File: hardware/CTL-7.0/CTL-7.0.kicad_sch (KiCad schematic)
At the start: 18 parts, among them J2 Left, J3 Right, U1 STM32H750VBTx, U2 AMS1117-3.3, Y1 32.768K, Y2 25MHz

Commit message: modified:   Ferrite Transformer Calculation.xlsx 	modified:   archive/Peripheral Migration ESP32S3-STM32H7.md 	renamed:    archive/PR_ 0201_2026.docx -> archive/Purchase 20260201.docx 	new file:   archive/Purchase 20260720.docx 	new file:   archive/Purchase Plan/bom.csv 	new file:   archive/Purchase Plan/bom.xlsx 	new file:   archive/Purchase Recaps.xlsx 	modified:   archive/REM - Vsense.xlsx 	new file:   archive/datasheets/SPC7040.PDF 	new file:   archive/datasheets/rm0433-stm32h742-stm32h743-753-and-stm32h750-value-line-advanced-armbased-32bit-mcus-stmicroelectronics.pdf 	new file:   archive/refferences/MiniSTM32H7xx-master/.gitattributes 	new file:   archive/refferences/MiniSTM32H7xx-master/.gitignore 	new file:   archive/refferences/MiniSTM32H7xx-master/Datasheet/MCU/DM00287603_ZHV2.pdf 	new file:   "archive/refferences/MiniSTM32H7xx-master/Datasheet/MCU/ES0396_STM32H750xB\345\222\214STM32H753xI\345\215\225\347\211\207\346\234\272\347\232\204\345\261\200\351\231\220\346\200\247.pdf" 	new file:   "archive/refferences/MiniSTM32H7xx-master/Datasheet/MCU/PM0253_STM32F7\345\222\214 STM32H7\345\215\225\347\211\207\346\234\272\347\274\226\347\250\213\346\211\213\345\206\214.pdf" 	new file:   "archive/refferences/MiniSTM32H7xx-master/Datasheet/MCU/RM0433_STM32H7x3\345\222\214STM32H750\345\215\225\347\211\207\346\234\272\345\217\202\350\200\203\346\211\213\345\206\214.pdf" 	new file:   archive/refferences/MiniSTM32H7xx-master/Datasheet/MCU/STM32H743VI_Datasheet.pdf 	new file:   archive/refferences/MiniSTM32H7xx-master/Datasheet/MCU/STM32H750VB_Datasheet.pdf 	new file:   archive/refferences/MiniSTM32H7xx-master/Datasheet/MKESD0402MS05.PDF 	new file:   archive/refferences/MiniSTM32H7xx-master/Datasheet/ST7735S_V1.5_20150303.pdf 	new file:   archive/refferences/MiniSTM32H7xx-master/Datasheet/SY8088AAC.PDF 	new file:   archive/refferences/MiniSTM32H7xx-master/Datasheet/Sensor/OV2640-camera module.pdf 	new file:   archive/refferences/MiniSTM32H7xx-master/Datasheet/Sensor/OV26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
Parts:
- removed C1, C3: 10u, Capacitor_Tantalum_SMD:CP_EIA-3528-12_Kemet-T, symbol Device:C_Polarized
- removed C2, C4: 100n, Capacitor_SMD:C_0805_2012Metric, symbol Device:C
- removed C5, C6: 10p, Capacitor_SMD:C_0805_2012Metric, symbol Device:C
- removed C7, C8: 20p, Capacitor_SMD:C_0805_2012Metric, symbol Device:C
- removed H1, H2, H3, H4: MountingHole_Pad, MountingHole:MountingHole_3mm_Pad, symbol Mechanical:MountingHole_Pad
- removed J2: Left, Connector_PinHeader_2.54mm:PinHeader_2x22_P2.54mm_Vertical, symbol Connector_Generic:Conn_02x22_Odd_Even
- removed J3: Right, Connector_PinHeader_2.54mm:PinHeader_2x22_P2.54mm_Vertical, symbol Connector_Generic:Conn_02x22_Odd_Even
- removed U1: STM32H750VBTx, Package_QFP:LQFP-100_14x14mm_P0.5mm, symbol MCU_ST_STM32H7:STM32H750VBTx
- removed U2: AMS1117-3.3, Package_TO_SOT_SMD:SOT-223-3_TabPin2, symbol Regulator_Linear:AMS1117-3.3
- removed Y1: 32.768K, Crystal:Crystal_SMD_3215-2Pin_3.2x1.5mm, symbol Device:Crystal
- removed Y2: 25MHz, Crystal:Crystal_SMD_5032-2Pin_5.0x3.2mm, symbol Device:Crystal
- added U1: H750, Core:STM32H750_v1, symbol core:STM32H750VBTx
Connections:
- net GND: now also U1.10 (GND), U1.19 (GND), U1.26 (GND), U1.49 (GND), U1.74 (GND), U1.99 (GND)
- new net: U1.100 (+3.3V_OUT), U1.11 (+3.3V_OUT), U1.27 (+3.3V_OUT), U1.75 (+3.3V_OUT)
- new net CTL_RLY1: U1.29 (A.05)
- new net CTL_RLY2: U1.30 (A.06)
- new net MSD1: U1.24 (A.02)
- new net MSD2: U1.25 (A.03)
- new net OPTO: U1.28 (A.04)
- new net PWM_EN: U1.31 (A.07)
- new net SENS_COAG: U1.23 (A.01)
- new net SENS_CUT: U1.22 (A.00)

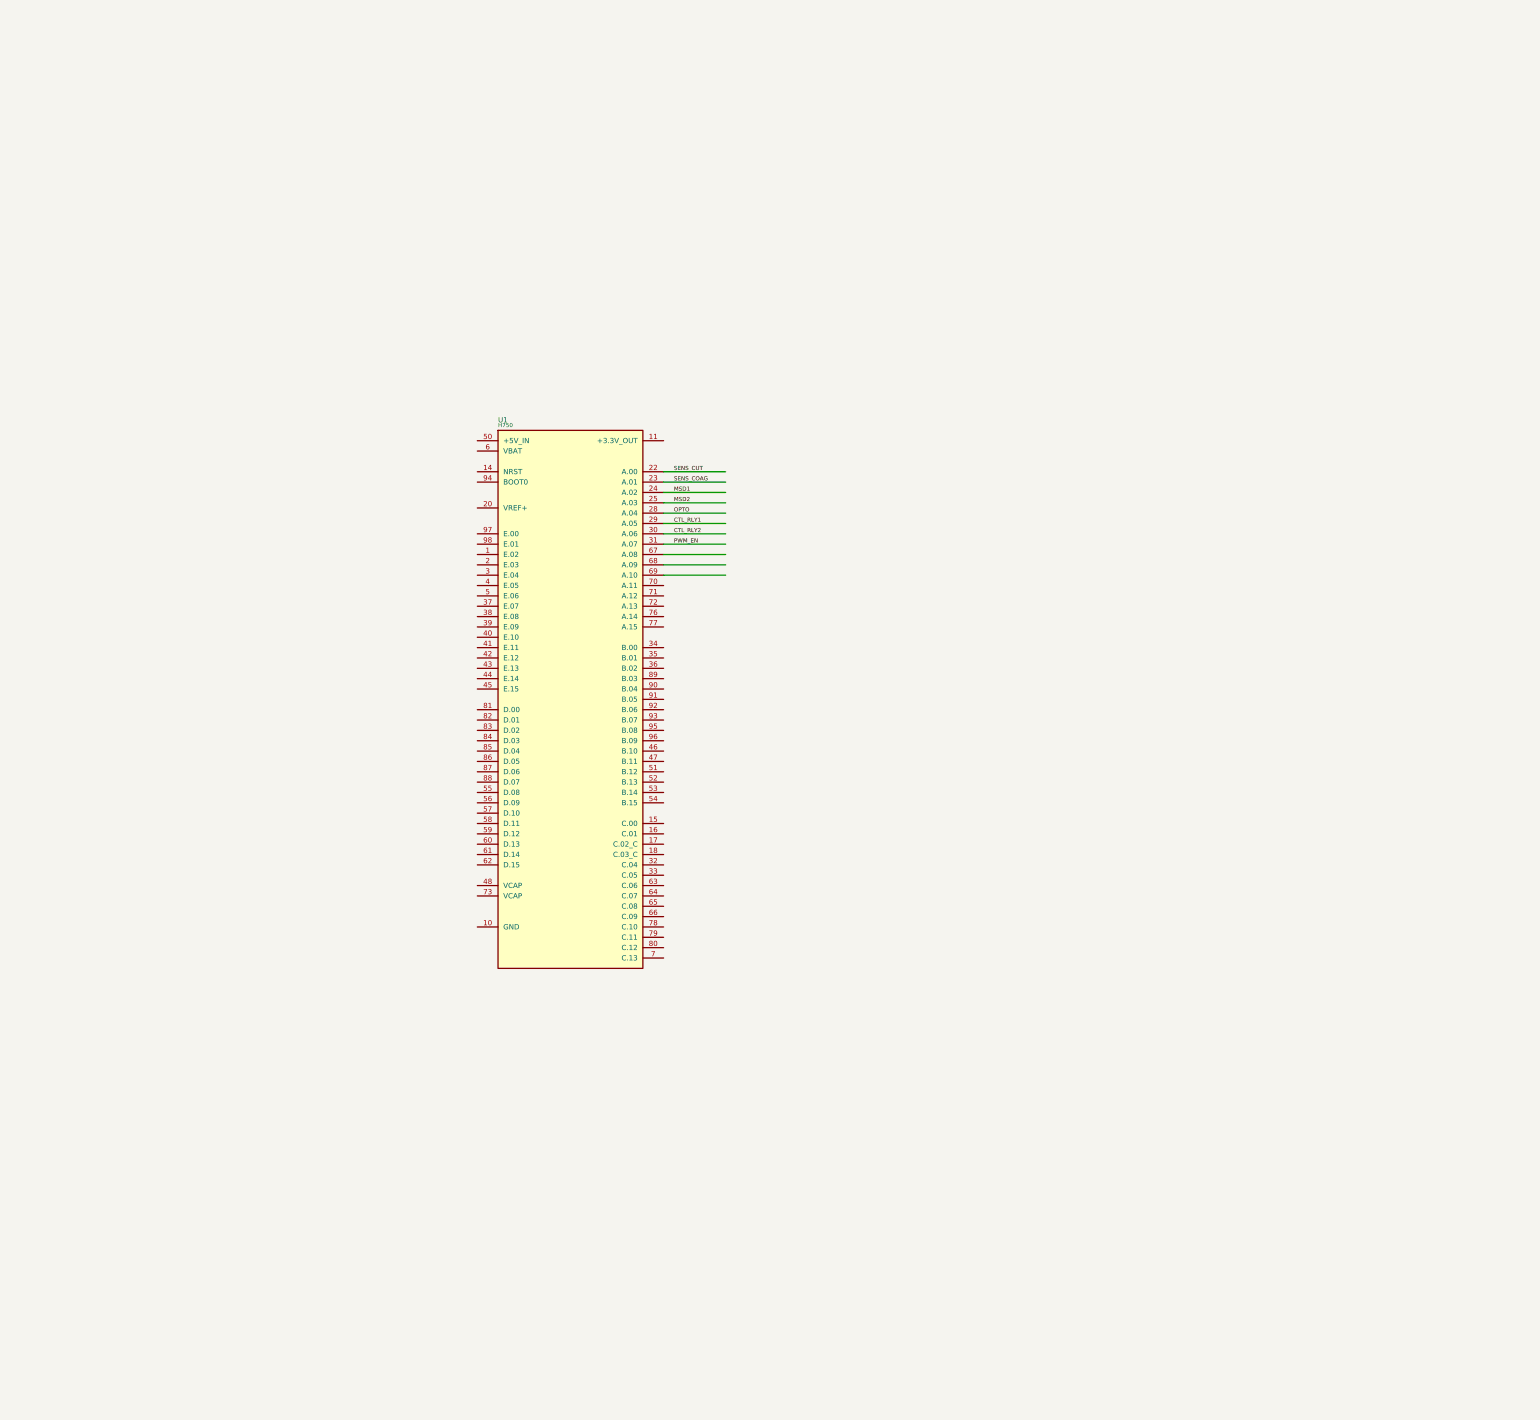
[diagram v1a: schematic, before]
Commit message: modified:   archive/Peripheral Migration ESP32S3-STM32H7.md 	new file:   archive/refferences/STM32H750xB pin definition.xlsx 	new file:   archive/refferences/STM32H750xB_pin_definition-TIM_LPTIM_HRTIM.xlsx 	new file:   archive/refferences/pin alternatives.xlsx 	new file:   firmware/core-h750/.cproject 	new file:   firmware/core-h750/.mxproject 	new file:   firmware/core-h750/.osx.project 	new file:   firmware/core-h750/.project 	new file:   firmware/core-h750/.settings/language.settings.xml 	new file:   firmware/core-h750/.settings/org.eclipse.core.resources.prefs 	new file:   firmware/core-h750/.settings/stm32cubeide.project.prefs 	new file:   firmware/core-h750/Debug/Drivers/STM32H7xx_HAL_Driver/Src/stm32h7xx_hal.cyclo 	new file:   firmware/core-h750/Debug/Drivers/STM32H7xx_HAL_Driver/Src/stm32h7xx_hal.su 	new file:   firmware/core-h750/Debug/Drivers/STM32H7xx_HAL_Driver/Src/stm32h7xx_hal_cortex.cyclo 	new file:   firmware/core-h750/Debug/Drivers/STM32H7xx_HAL_Driver/Src/stm32h7xx_hal_cortex.su 	new file:   firmware/core-h750/Debug/Drivers/STM32H7xx_HAL_Driver/Src/stm32h7xx_hal_dma.cyclo 	new file:   firmware/core-h750/Debug/Drivers/STM32H7xx_HAL_Driver/Src/stm32h7xx_hal_dma.su 	new file:   firmware/core-h750/Debug/Drivers/STM32H7xx_HAL_Driver/Src/stm32h7xx_hal_dma_ex.cyclo 	new file:   firmware/core-h750/Debug/Drivers/STM32H7xx_HAL_Driver/Src/stm32h7xx_hal_dma_ex.su 	new file:   firmware/core-h750/Debug/Drivers/STM32H7xx_HAL_Driver/Src/stm32h7xx_hal_exti.cyclo 	new file:   firmware/core-h750/Debug/Drivers/STM32H7xx_HAL_Driver/Src/stm32h7xx_hal_exti.su 	new file:   firmware/core-h750/Debug/Drivers/STM32H7xx_HAL_Driver/Src/stm32h7xx_hal_flash.cyclo 	new file:   firmware/core-h750/Debug/Drivers/STM32H7xx_HAL_Driver/Src/stm32h7xx_hal_flash.su 	new file:   firmware/core-h750/Debug/Drivers/STM32H7xx_HAL_Driver/Src/stm32h7xx_hal_flash_ex.cyclo 	new file:   firmware/core-h750/Debug/Drivers/STM32H7xx_HAL_Driver/Src/stm32h7xx_hal_flash_ex.su 	new file:   firmware/core-h750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
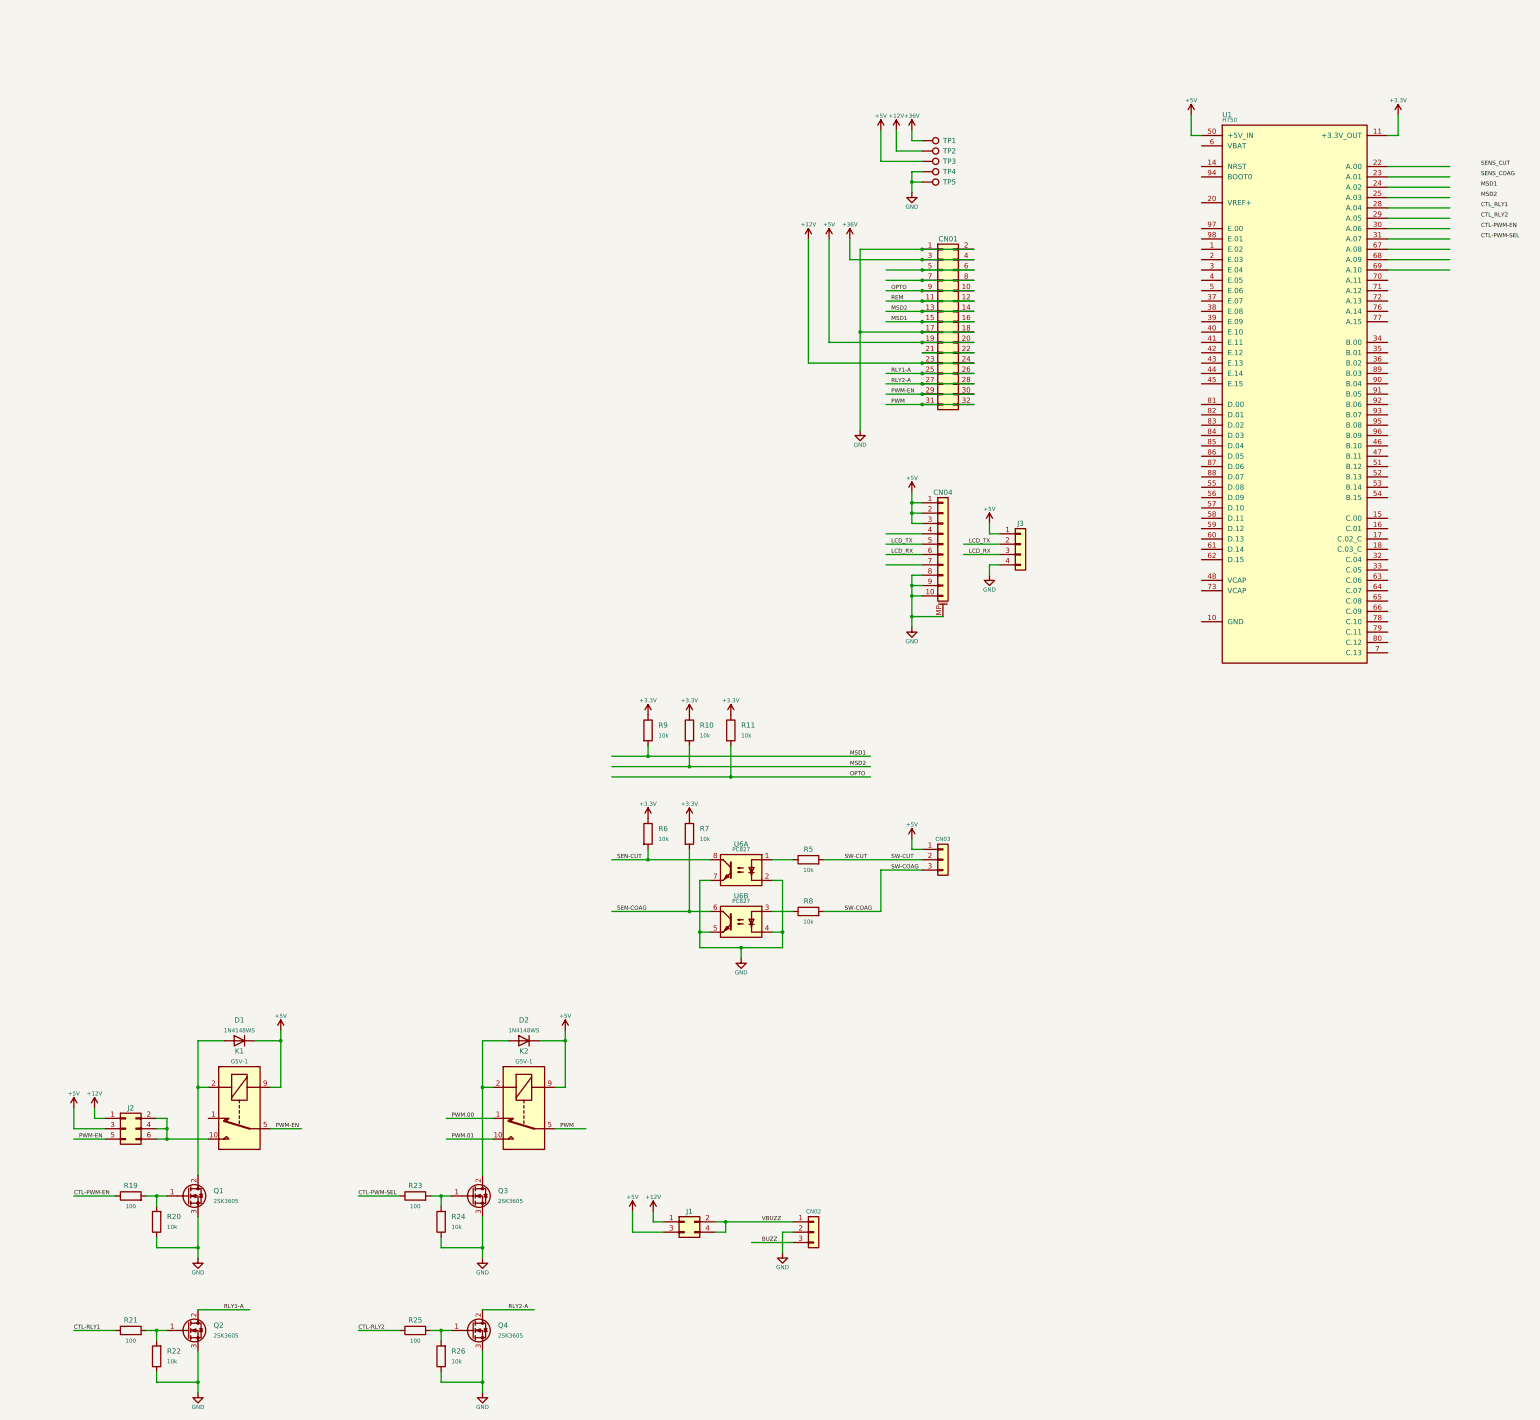
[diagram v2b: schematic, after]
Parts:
- added CN01: Conn_02x16_Odd_Even, Connector_PinHeader_2.54mm:PinHeader_2x16_P2.54mm_Vertical, symbol Connector_Generic:Conn_02x16_Odd_Even
- added CN02, CN03: Conn_01x03, Connector_JST:JST_XH_B3B-XH-A_1x03_P2.50mm_Vertical, symbol Connector_Generic:Conn_01x03
- added CN04: (no value), Connector_FFC-FPC:TE_1-84952-0_1x10-1MP_P1.0mm_Horizontal, symbol Connector_Generic_MountingPin:Conn_01x10_MountingPin
- added D1, D2: 1N4148WS, Diode_SMD:D_SOD-323, symbol Diode:1N4148WS
- added J1: Conn_02x02_Odd_Even, Connector_PinHeader_2.54mm:PinHeader_2x02_P2.54mm_Vertical_SMD, symbol Connector_Generic:Conn_02x02_Odd_Even
- added J2: Conn_02x03_Odd_Even, Connector_PinHeader_2.54mm:PinHeader_2x03_P2.54mm_Vertical_SMD, symbol Connector_Generic:Conn_02x03_Odd_Even
- added J3: Conn_01x04, Connector_PinHeader_2.54mm:PinHeader_1x04_P2.54mm_Vertical, symbol Connector_Generic:Conn_01x04
- added K1, K2: G5V-1, Relay_THT:Relay_SPDT_Omron_G5V-1, symbol Relay:G5V-1
- added Q1, Q2, Q3, Q4: 2SK3605, Package_TO_SOT_SMD:SOT-89-3, symbol Transistor_FET:2SK3065
- added R10, R11, R20, R22, R24, R26, R5, R6, R7, R8, R9: 10k, Resistor_SMD:R_0805_2012Metric, symbol Device:R
- added R19, R21, R23, R25: 100, Resistor_SMD:R_0805_2012Metric, symbol Device:R
- added TP1, TP2, TP3, TP4, TP5: TestPoint, TestPoint:TestPoint_THTPad_2.2225x2.2225mm_Drill1.5mm, symbol Connector:TestPoint
- added U6: PC827, Package_DIP:DIP-8_W7.62mm_Socket, symbol Isolator:PC827
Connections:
- net CTL_RLY1: no longer U1.29 (A.05)
- net CTL_RLY2: no longer U1.30 (A.06)
- net GND: now also CN01.1 (Pin_1), CN01.17 (Pin_17), CN01.18 (Pin_18), CN01.2 (Pin_2), CN02.2 (Pin_2), CN04.10 (Pin_10), CN04.8 (Pin_8), CN04.9 (Pin_9), CN04.MP (MountPin), J3.4 (Pin_4), Q1.3 (S), Q2.3 (S), Q3.3 (S), Q4.3 (S), R20.1, R22.1, R24.1, R26.1, TP4.1, TP5.1, U6.2, U6.4, U6.5, U6.7
- net MSD1: now also CN01.15 (Pin_15), CN01.16 (Pin_16), R9.2; no longer U1.24 (A.02)
- net MSD2: now also CN01.13 (Pin_13), CN01.14 (Pin_14), R10.2; no longer U1.25 (A.03)
- net OPTO: now also CN01.10 (Pin_10), CN01.9 (Pin_9), R11.2; no longer U1.28 (A.04)
- net SENS_COAG: no longer U1.23 (A.01)
- net SENS_CUT: no longer U1.22 (A.00)
- net +3.3V: now reaches U1.100 (+3.3V_OUT), U1.11 (+3.3V_OUT), U1.27 (+3.3V_OUT), U1.75 (+3.3V_OUT)
- net +3.3V: now also R10.1, R11.1, R6.1, R7.1, R9.1
- net +5V: now reaches U1.50 (+5V_IN)
- net +5V: now also CN01.19 (Pin_19), CN01.20 (Pin_20), CN03.1 (Pin_1), CN04.1 (Pin_1), CN04.2 (Pin_2), CN04.3 (Pin_3), D1.1 (K), D2.1 (K), J1.3 (Pin_3), J2.3 (Pin_3), J3.1 (Pin_1), K1.9, K2.9, TP3.1
- net PWM_EN: no longer names the net of U1.31 (A.07)
- new net: D2.2 (A), K2.2, Q3.2 (D)
- new net: CN01.21 (Pin_21), CN01.22 (Pin_22)
- new net: CN01.5 (Pin_5), CN01.6 (Pin_6)
- new net: CN01.7 (Pin_7), CN01.8 (Pin_8)
- new net: Q3.1 (G), R23.2, R24.2
- new net: Q4.1 (G), R25.2, R26.2
- new net: R8.1, U6.3
- new net: R5.1, U6.1
- new net: Q1.1 (G), R19.2, R20.2
- new net: Q2.1 (G), R21.2, R22.2
- new net: D1.2 (A), K1.2, Q1.2 (D)
- new net: J2.2 (Pin_2), J2.4 (Pin_4), J2.6 (Pin_6), K1.10
- new net +12V: CN01.23 (Pin_23), CN01.24 (Pin_24), J1.1 (Pin_1), J2.1 (Pin_1), TP2.1
- new net +36V: CN01.3 (Pin_3), CN01.4 (Pin_4), TP1.1
- new net BUZZ: CN02.3 (Pin_3)
- new net CTL-PWM-EN: R19.1
- new net CTL-PWM-SEL: R23.1
- new net CTL-RLY1: R21.1
- new net CTL-RLY2: R25.1
- new net LCD_RX: CN04.6 (Pin_6), J3.3 (Pin_3)
- new net LCD_TX: CN04.5 (Pin_5), J3.2 (Pin_2)
- new net PWM: CN01.31 (Pin_31), CN01.32 (Pin_32), K2.5, K2.6
- new net PWM-EN: CN01.29 (Pin_29), CN01.30 (Pin_30), J2.5 (Pin_5), K1.5, K1.6
- new net PWM.00: K2.1
- new net PWM.01: K2.10
- new net REM: CN01.11 (Pin_11), CN01.12 (Pin_12)
- new net RLY1-A: CN01.25 (Pin_25), CN01.26 (Pin_26), Q2.2 (D)
- new net RLY2-A: CN01.27 (Pin_27), CN01.28 (Pin_28), Q4.2 (D)
- new net SEN-COAG: R7.2, U6.6
- new net SEN-CUT: R6.2, U6.8
- new net SW-COAG: CN03.3 (Pin_3), R8.2
- new net SW-CUT: CN03.2 (Pin_2), R5.2
- new net VBUZZ: CN02.1 (Pin_1), J1.2 (Pin_2), J1.4 (Pin_4)
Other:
- moved on the sheet: U1
